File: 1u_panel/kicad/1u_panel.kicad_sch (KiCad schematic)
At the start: 0 parts

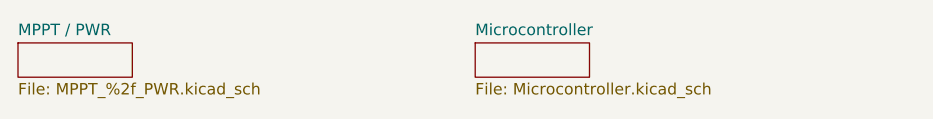
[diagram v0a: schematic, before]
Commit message: Switch to PSAS naming convention!
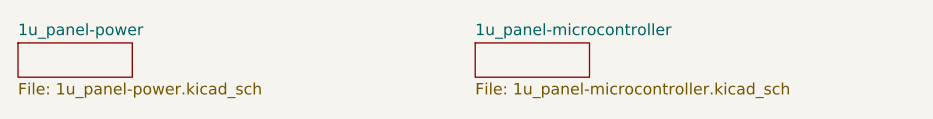
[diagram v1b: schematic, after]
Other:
- sheet MPPT / PWR renamed 1u_panel-power
- sheet Microcontroller renamed 1u_panel-microcontroller
- sheet 1u_panel-microcontroller: file Microcontroller.kicad_sch -> 1u_panel-microcontroller.kicad_sch
- sheet 1u_panel-power: file MPPT_%2f_PWR.kicad_sch -> 1u_panel-power.kicad_sch
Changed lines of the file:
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@@
     (stroke (width 0) (type solid))
     (fill (color 0 0 0 0.0000))
-    (property "Sheetname" "MPPT / PWR" (at 25.4 24.6884 0)
+    (property "Sheetname" "1u_panel-power" (at 25.4 24.6884 0)
       (effects (font (size 1.27 1.27)) (justify left bottom))
     )
-    (property "Sheetfile" "MPPT_%2f_PWR.kicad_sch" (at 25.4 29.7946 0)
+    (property "Sheetfile" "1u_panel-power.kicad_sch" (at 25.4 29.7946 0)
       (effects (font (size 1.27 1.27)) (justify left top))
     )
@@
     (stroke (width 0) (type solid))
     (fill (color 0 0 0 0.0000))
-    (property "Sheetname" "Microcontroller" (at 76.2 24.6884 0)
+    (property "Sheetname" "1u_panel-microcontroller" (at 76.2 24.6884 0)
       (effects (font (size 1.27 1.27)) (justify left bottom))
     )
-    (property "Sheetfile" "Microcontroller.kicad_sch" (at 76.2 29.7946 0)
+    (property "Sheetfile" "1u_panel-microcontroller.kicad_sch" (at 76.2 29.7946 0)
       (effects (font (size 1.27 1.27)) (justify left top))
     )

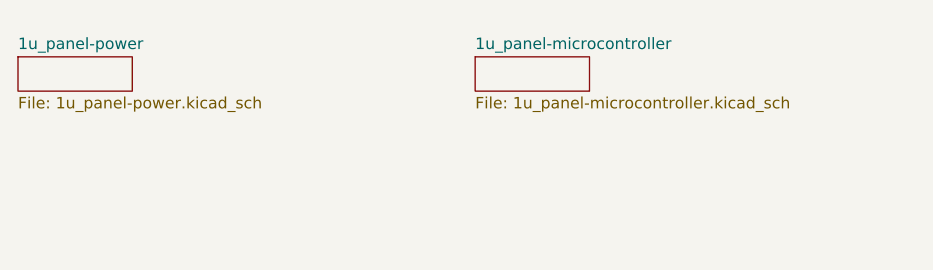
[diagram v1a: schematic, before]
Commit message: Fixed R12 value to make VOUT to 8.4V max. Was at 8.6V max. Also cleaned up some EAGLE import issues, mostly text size and labels.
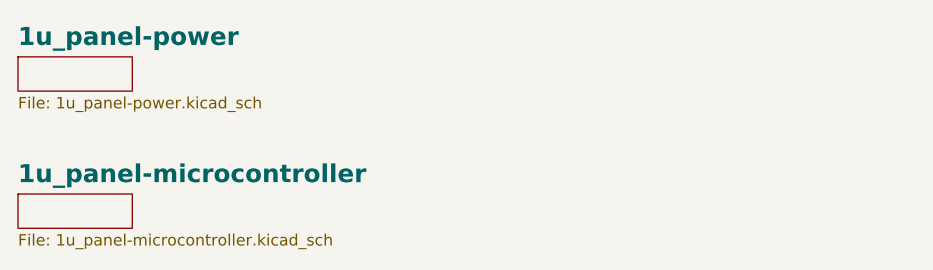
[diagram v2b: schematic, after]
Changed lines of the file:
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@@
     (stroke (width 0) (type solid))
     (fill (color 0 0 0 0.0000))
-    (property "Sheetname" "1u_panel-power" (at 25.4 24.6884 0)
-      (effects (font (size 1.27 1.27)) (justify left bottom))
+    (property "Sheetname" "1u_panel-power" (at 25.4 24.3234 0)
+      (effects (font (size 2 2) bold) (justify left bottom))
     )
     (property "Sheetfile" "1u_panel-power.kicad_sch" (at 25.4 29.7946 0)
@@
     )
   )
-  (sheet (at 76.2 25.4) (size 12.7 3.81) (fields_autoplaced)
+  (sheet (at 25.4 40.64) (size 12.7 3.81) (fields_autoplaced)
     (stroke (width 0) (type solid))
     (fill (color 0 0 0 0.0000))
-    (property "Sheetname" "1u_panel-microcontroller" (at 76.2 24.6884 0)
-      (effects (font (size 1.27 1.27)) (justify left bottom))
+    (property "Sheetname" "1u_panel-microcontroller" (at 25.4 39.5634 0)
+      (effects (font (size 2 2) bold) (justify left bottom))
     )
-    (property "Sheetfile" "1u_panel-microcontroller.kicad_sch" (at 76.2 29.7946 0)
+    (property "Sheetfile" "1u_panel-microcontroller.kicad_sch" (at 25.4 45.0346 0)
       (effects (font (size 1.27 1.27)) (justify left top))
     )

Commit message: Beginning of the v6.0 solar boards. Lots of ways to go.
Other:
- title: (none) -> OreSat Solar Module (for Frame 2.0)
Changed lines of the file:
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@@
 (kicad_sch (version 20230121) (generator eeschema)
-  (paper "A4")
+  (paper "USLedger")
+  (title_block
+    (title "OreSat Solar Module (for Frame 2.0)")
+    (date "2023-12-20")
+    (rev "6.0")
+  )
   (sheet (at 25.4 25.4) (size 12.7 3.81) (fields_autoplaced)
     (stroke (width 0) (type solid))
